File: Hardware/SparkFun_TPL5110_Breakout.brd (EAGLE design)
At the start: 1 part

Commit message: Completes schematic and board design, adds buzzard labels
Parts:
- added D1: RED, SparkFun-LED:LED-0603
- added FD1, FD2, FD3, FD4: FIDUCIALUFIDUCIAL, SparkFun-Aesthetics:FIDUCIAL-MICRO
- added H1, H2, H4: STAND-OFFTIGHT, SparkFun-Hardware:STAND-OFF-TIGHT
- added J1: (no value), SparkFun-Connectors:JST-2-SMD
- added J2: (no value), SparkFun-Connectors:1X05_NO_SILK
- added JP2: LED, SparkFun-Jumpers:SMT-JUMPER_2_NC_TRACE_SILK
- added LOGO1: SFE_LOGO_NAME.1_INCH, SparkFun-Aesthetics:SFE_LOGO_NAME_.1
- added LOGO2: OSHW-LOGOS, SparkFun-Aesthetics:OSHW-LOGO-S
- added Q1: 1.1A/60V/600mΩ, SparkFun-DiscreteSemi:SOT23-3
- added R1, R2, R3, R4, R5: 5.6k, SparkFun-Resistors:0603
- added R6: 330, SparkFun-Resistors:0603
- added R7: (no value), SparkFun-Resistors:0603
- added R8: (no value), SparkFun-Resistors:AXIAL-0.3
- added S1: MOMENTARY-SWITCH-SPST-SMD-5.2MM-TALL, SparkFun-Switches:TACTILE_SWITCH_SMD_5.2MM
- added SW1: DIP-06, SparkFun-Switches:DIPSWITCH-06-SMD
- added U$1: (no value), DONE:DONE0
- added U$10: (no value), 30:30S0
- added U$11: (no value), 1.15:1#15S0
- added U$12: (no value), 45:45S0
- added U$13: (no value), LED:LED0
- added U$14: (no value), CUSTOM:CUSTOM0
- added U$15: (no value), time:TIME#OFF0
- added U$2, U$4: (no value), Labels:GND-03
- added U$3: (no value), VDDOUT:V_OUT0
- added U$5: (no value), VDD:VDD0
- added U$6: (no value), Nano Power:NANO_POWER0
- added U$7: (no value), Switch:SWITCH0
- added U$8: (no value), 15s:15S0
- added U$9: (no value), 20:20S0
- added U1: TPL5110, SparkFun-IC-Power:SOT23-6
- moved FRAME1 19.5 mm to (-10.4, -15.5)
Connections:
- new net DELAY: S1.3, SW1.1, SW1.2, SW1.3, SW1.4, SW1.5, SW1.6, U1.3
- new net DONE: J2.4, U1.4
- new net DRV: Q1.1, U1.5
- new net GND: J1.1, J2.1, J2.3, R1.2, R2.2, R3.2, R4.2, R5.2, R6.1, R7.1, R8.P$2, U1.2
- new net N$1: D1.C, R6.2
- new net N$11: D1.A, JP2.1
- new net N$4: R1.1, SW1.12
- new net N$5: R2.1, SW1.11
- new net N$6: R3.1, SW1.10
- new net N$7: R4.1, SW1.9
- new net N$8: R5.1, SW1.8
- new net N$9: R7.2, R8.P$1, SW1.7
- new net VDD: J1.2, J2.5, JP2.2, Q1.3, S1.1, U1.1, U1.6
- new net VDD_OUT: J2.2, Q1.2
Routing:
- net VDD: track 0.00 -> 51.2 mm, vias 0 -> 1
- net DELAY: track 0.00 -> 31.7 mm, vias 0 -> 2
- net N$9: track 0.00 -> 26.7 mm
- net N$8: track 0.00 -> 19.1 mm
- net N$7: track 0.00 -> 17.5 mm
- net N$6: track 0.00 -> 15.5 mm
- net N$5: track 0.00 -> 13.9 mm
- net DONE: track 0.00 -> 11.8 mm, vias 0 -> 1
- net N$4: track 0.00 -> 8.57 mm
- net DRV: track 0.00 -> 7.59 mm, vias 0 -> 2
- net VDD_OUT: track 0.00 -> 6.67 mm
- net N$11: track 0.00 -> 5.34 mm, vias 0 -> 1
- net N$1: track 0.00 -> 1.72 mm
- added copper zone on layer 1, net GND
- added copper zone on layer 16, net GND
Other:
- board outline added: 25.4 x 25.4 mm
- board text added: "Elias Santistevan"
- board text added: "v10"

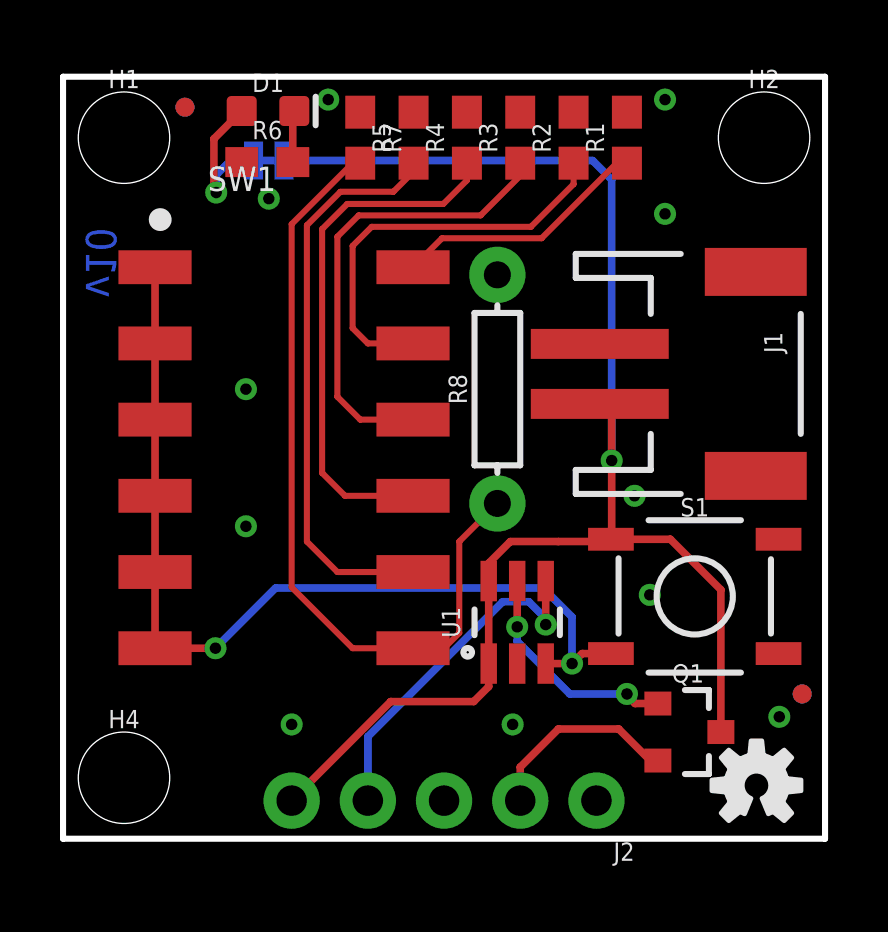
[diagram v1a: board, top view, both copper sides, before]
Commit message: Updates buzzard labels, changes 5 pin header to 6 pin
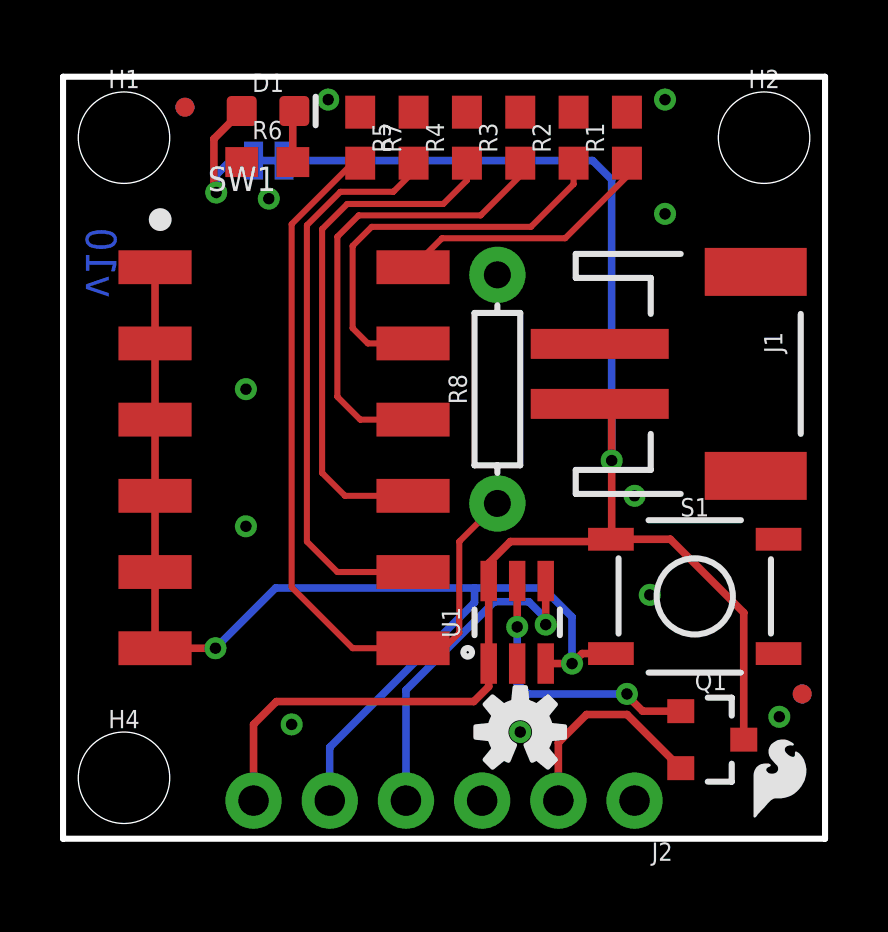
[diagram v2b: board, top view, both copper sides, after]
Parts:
- added LOGO3: SFE_LOGO_FLAME.1_INCH, SparkFun-Aesthetics:SFE_LOGO_FLAME_.1
- added U$16: (no value), M_DRIVE:DRV0
- J2: device SparkFun-Connectors:1X05_NO_SILK -> SparkFun-Connectors:1X06_NO_SILK
- U$3: device VDDOUT:V_OUT0 -> VDDOUT:VOUT0
- moved LOGO2 8.07 mm to (15.2, 3.56)
- moved U$4 1.40 mm to (14.0, 1.63)
- moved U$3 1.35 mm to (16.5, 1.63)
- moved U$5 1.27 mm to (6.35, 1.78)
- moved J2 1.27 mm to (19.1, 1.27)
- moved U$2 1.27 mm to (19.1, 1.63)
- moved U$1 1.22 mm to (11.4, 1.68)
- moved Q1 0.80 mm to (21.6, 3.30)
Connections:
- net DRV renamed !DRV
- removed net DELAY: S1.3, SW1.1, SW1.2, SW1.3, SW1.4, SW1.5, SW1.6, U1.3
- new net DELAY/M_DRIVE: J2.5, S1.3, SW1.1, SW1.2, SW1.3, SW1.4, SW1.5, SW1.6, U1.3
- net VDD: now also J2.6; no longer J2.5
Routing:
- net DELAY/M_DRIVE: track 0.00 -> 40.8 mm, vias 0 -> 2
- net DELAY: track 31.7 -> 0.00 mm, vias 2 -> 0
- net VDD: track 51.2 -> 54.5 mm
- net !DRV: track 7.59 -> 9.27 mm

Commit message: Adds additional labels to switches, increases trace width of VDD
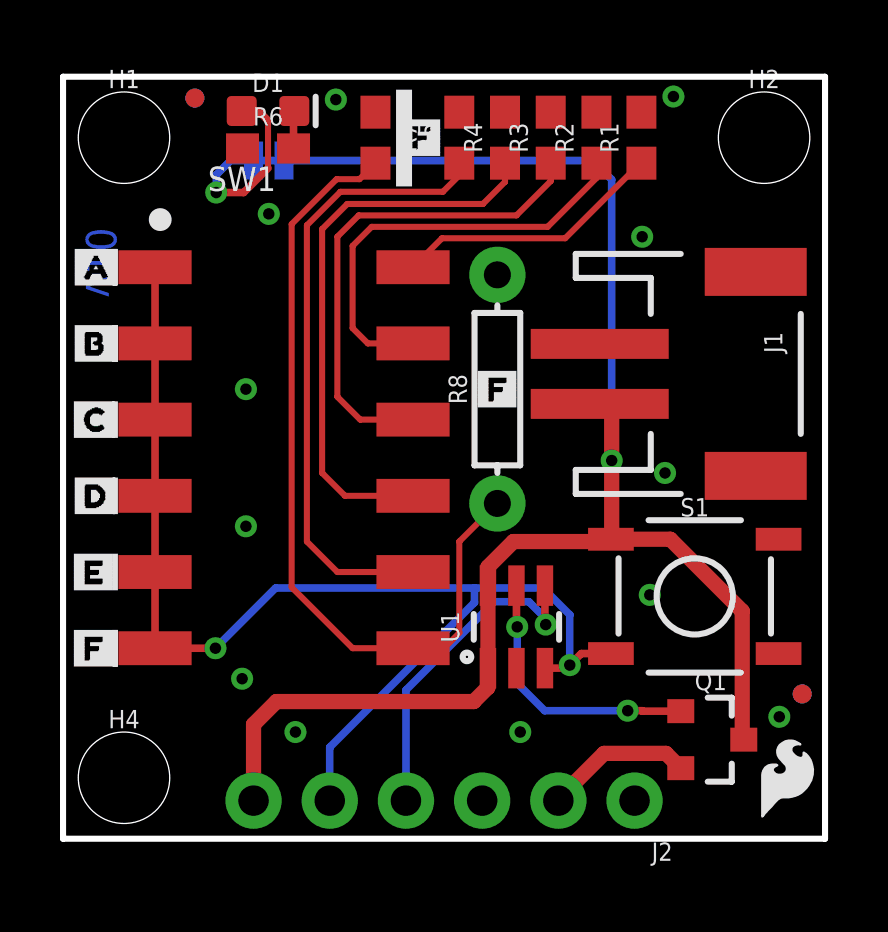
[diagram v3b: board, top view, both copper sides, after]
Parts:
- added U$17, U$25: (no value), RES_LABELS:A0
- added U$18, U$26: (no value), RES_LABELS:B1
- added U$19, U$27: (no value), RES_LABELS:C2
- added U$20, U$28: (no value), RES_LABELS:D3
- added U$21, U$29: (no value), RES_LABELS:E4
- added U$22, U$23, U$24, U$30: (no value), RES_LABELS:F5
- moved LOGO2 16.9 mm to (20.6, 19.6), flipped to the bottom, turned to 90 degrees
- moved R5 1.52 mm to (13.2, 23.4)
- moved R4 1.27 mm to (14.7, 23.4)
- moved R3 1.02 mm to (16.3, 23.4)
- moved R2 0.76 mm to (17.8, 23.4)
- moved R7 0.51 mm to (10.4, 23.4)
- moved R1 0.48 mm to (19.3, 23.4)
- moved R6 0.46 mm to (6.83, 23.0)
- moved FD1 0.45 mm to (4.39, 24.7)
- moved FD2 0.45 mm to (4.39, 24.7)
- moved LOGO3 0.25 mm to (24.1, 2.03)
- moved U1 0.15 mm to (15.1, 7.06)
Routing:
- net VDD_OUT: track 7.14 -> 4.97 mm
- net N$8: track 19.1 -> 20.7 mm
- net N$11: track 5.34 -> 6.69 mm
- net N$7: track 17.5 -> 18.8 mm
- net N$6: track 15.5 -> 16.6 mm
- net N$5: track 13.9 -> 14.5 mm
- net N$9: track 26.7 -> 27.2 mm

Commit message: Alignes swtich silk, adds "in/out" silk, increases size of product name silk
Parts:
- added U$31, U$33: (no value), IN_OUT:IN0
- added U$32, U$34: (no value), IN_OUT:OUT1
- R1: value 5.6k -> 16.2k
- R2: value 5.6k -> 22k
- U$10: device 30:30S0 -> time:30M2
- U$11: device 1.15:1#15S0 -> time:1HR3
- U$12: device 45:45S0 -> time:2HR4
- U$8: device 15s:15S0 -> time:1M0
- U$9: device 20:20S0 -> time:30S4
- moved LOGO1 12.5 mm to (15.5, 22.4), turned to 0 degrees
- moved U$11 3.61 mm to (6.58, 11.4)
- moved U$9 3.59 mm to (6.60, 19.1)
- moved U$12 3.45 mm to (6.55, 8.89)
- moved U$8 3.45 mm to (6.55, 16.5)
- moved U$6 3.06 mm to (23.9, 6.10)
- moved U$10 2.62 mm to (6.53, 14.0)
- moved U$15 2.55 mm to (9.65, 7.37)
- moved LOGO2 2.55 mm to (23.1, 19.8), turned to 0 degrees
- moved U$14 2.32 mm to (8.13, 6.35)
- moved U$7 1.98 mm to (21.8, 8.89)
